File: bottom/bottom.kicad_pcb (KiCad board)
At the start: 2 copper layers, 27.5 x 37.7 mm, 5 parts, among them P1 HLW4R-2C7LF, P2 CONN_5

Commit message: Change SDA and SCL lines.
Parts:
- P1: value HLW4R-2C7LF -> CONN_4
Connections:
- P1 pad 2: /SCL -> /SDA
- P1 pad 3: /SDA -> /SCL
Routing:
- net /SDA: track 9.94 -> 13.5 mm
- net /SCL: track 13.0 -> 11.4 mm
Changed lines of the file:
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@@
     (thickness 1.6)
     (drawings 33)
-    (tracks 10)
+    (tracks 12)
     (zones 0)
     (modules 5)
@@
   )
   (setup
-    (last_trace_width 0.4064)
+    (last_trace_width 0.2032)
     (user_trace_width 0.4064)
     (trace_clearance 0.2032)
@@
       (effects (font (size 0.75 0.75) (thickness 0.15)))
     )
-    (fp_text value HLW4R-2C7LF (at 4.160001 -4.25 180) (layer F.SilkS)
+    (fp_text value CONN_4 (at 4.160001 -4.25 180) (layer F.SilkS)
       (effects (font (size 0.75 0.75) (thickness 0.15)))
     )
@@
       (net 1 /VCC))
     (pad 3 thru_hole circle (at -0.5 -5.25 270) (size 1.3 1.3) (drill 0.7) (layers *.Cu *.Mask)
+      (net 3 /SCL))
+    (pad 2 thru_hole circle (at 0.5 -3.25 270) (size 1.3 1.3) (drill 0.7) (layers *.Cu *.Mask)
       (net 2 /SDA))
-    (pad 2 thru_hole circle (at 0.5 -3.25 270) (size 1.3 1.3) (drill 0.7) (layers *.Cu *.Mask)
-      (net 3 /SCL))
     (pad 1 thru_hole circle (at 1.5 -5.25 270) (size 1.3 1.3) (drill 0.7) (layers *.Cu *.Mask)
       (net 4 /GND))
@@
   (segment (start 211.1 137.639999) (end 212.339999 136.4) (width 0.762) (layer F.Cu) (net 1))
   (segment (start 212.339999 136.4) (end 222.6 136.4) (width 0.762) (layer F.Cu) (net 1))
-  (segment (start 222.1484 139.7) (end 222.6 139.7) (width 0.2032) (layer F.Cu) (net 2))
-  (segment (start 213.1 138.639999) (end 221.088399 138.639999) (width 0.2032) (layer F.Cu) (net 2))
-  (segment (start 221.088399 138.639999) (end 222.1484 139.7) (width 0.2032) (layer F.Cu) (net 2))
-  (segment (start 222.2448 143.2) (end 222.6 143.2) (width 0.2032) (layer F.Cu) (net 3))
-  (segment (start 211.1 139.639999) (end 218.684799 139.639999) (width 0.2032) (layer F.Cu) (net 3))
-  (segment (start 218.684799 139.639999) (end 222.2448 143.2) (width 0.2032) (layer F.Cu) (net 3))
+  (segment (start 211.1 139.226893) (end 211.1 139.639999) (width 0.2032) (layer F.Cu) (net 2))
+  (segment (start 212.785893 137.541) (end 211.1 139.226893) (width 0.2032) (layer F.Cu) (net 2))
+  (segment (start 219.9894 137.541) (end 212.785893 137.541) (width 0.2032) (layer F.Cu) (net 2))
+  (segment (start 222.1484 139.7) (end 219.9894 137.541) (width 0.2032) (layer F.Cu) (net 2))
+  (segment (start 222.6 139.7) (end 222.1484 139.7) (width 0.2032) (layer F.Cu) (net 2))
+  (segment (start 217.684799 138.639999) (end 213.1 138.639999) (width 0.2032) (layer F.Cu) (net 3))
+  (segment (start 222.6 143.2) (end 222.2448 143.2) (width 0.2032) (layer F.Cu) (net 3))
+  (segment (start 222.2448 143.2) (end 217.684799 138.639999) (width 0.2032) (layer F.Cu) (net 3))
   (segment (start 213.1 140.639999) (end 218.960001 146.5) (width 0.762) (layer F.Cu) (net 4))
   (segment (start 218.960001 146.5) (end 222.6 146.5) (width 0.762) (layer F.Cu) (net 4))

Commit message: Feature connector part names on the bottom board.
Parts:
- P1: value CONN_4 -> HLW4R-2C7LF
- P2: value CONN_5 -> BP167911-05340H0A
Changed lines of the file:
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@@
-(kicad_pcb (version 20171130) (host pcbnew "(5.0.0)")
+(kicad_pcb (version 20171130) (host pcbnew 5.1.3-ffb9f22~84~ubuntu18.04.1)
   (general
     (thickness 1.6)
@@
     (zone_45_only no)
     (trace_min 0.2032)
-    (segment_width 0.2)
-    (edge_width 0.1)
     (via_size 0.889)
     (via_drill 0.635)
@@
     (uvia_min_size 0.508)
     (uvia_min_drill 0.127)
+    (edge_width 0.1)
+    (segment_width 0.2)
     (pcb_text_width 0.3)
     (pcb_text_size 1.5 1.5)
@@
     (pad_to_mask_clearance 0)
     (aux_axis_origin 0 0)
-    (visible_elements 7FFFFFFF)
+    (visible_elements 7FFFEFFF)
     (pcbplotparams
       (layerselection 0x00030_ffffffff)
@@
     (uvia_dia 0.508)
     (uvia_drill 0.127)
+    (diff_pair_width 0.2032)
     (diff_pair_gap 0.25)
-    (diff_pair_width 0.2032)
     (add_net /GND)
     (add_net /MERGE_SENSE)
@@
       (effects (font (size 0.75 0.75) (thickness 0.15)))
     )
-    (fp_text value CONN_4 (at 4.160001 -4.25 180) (layer F.SilkS)
+    (fp_text value HLW4R-2C7LF (at 4.160001 -4.25 180) (layer F.SilkS)
       (effects (font (size 0.75 0.75) (thickness 0.15)))
     )
@@
       (effects (font (size 0.75 0.75) (thickness 0.15)))
     )
-    (fp_text value CONN_5 (at 0 -9.95 180) (layer F.SilkS) hide
+    (fp_text value BP167911-05340H0A (at -4.55 -1.239999 90) (layer F.SilkS)
       (effects (font (size 0.75 0.75) (thickness 0.15)))
     )

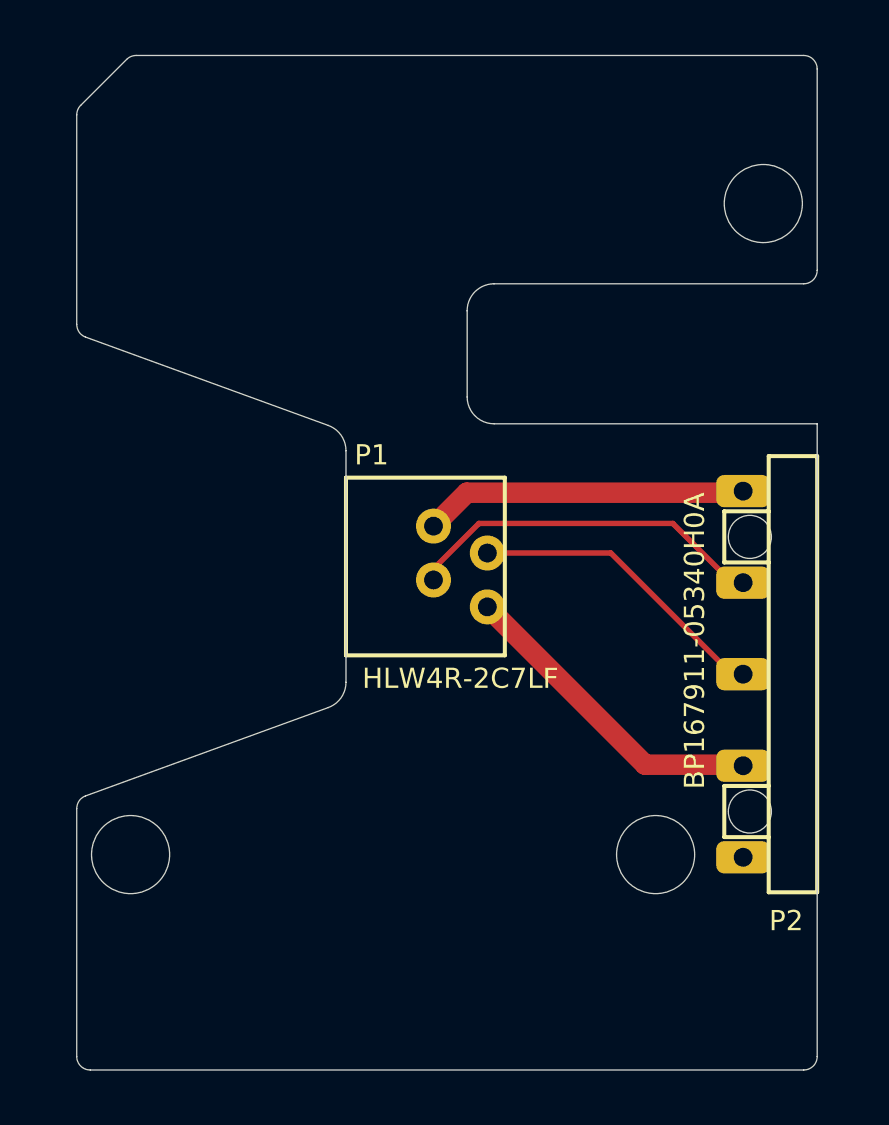
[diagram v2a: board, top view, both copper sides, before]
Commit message: Update bottom board according to new CAD files.
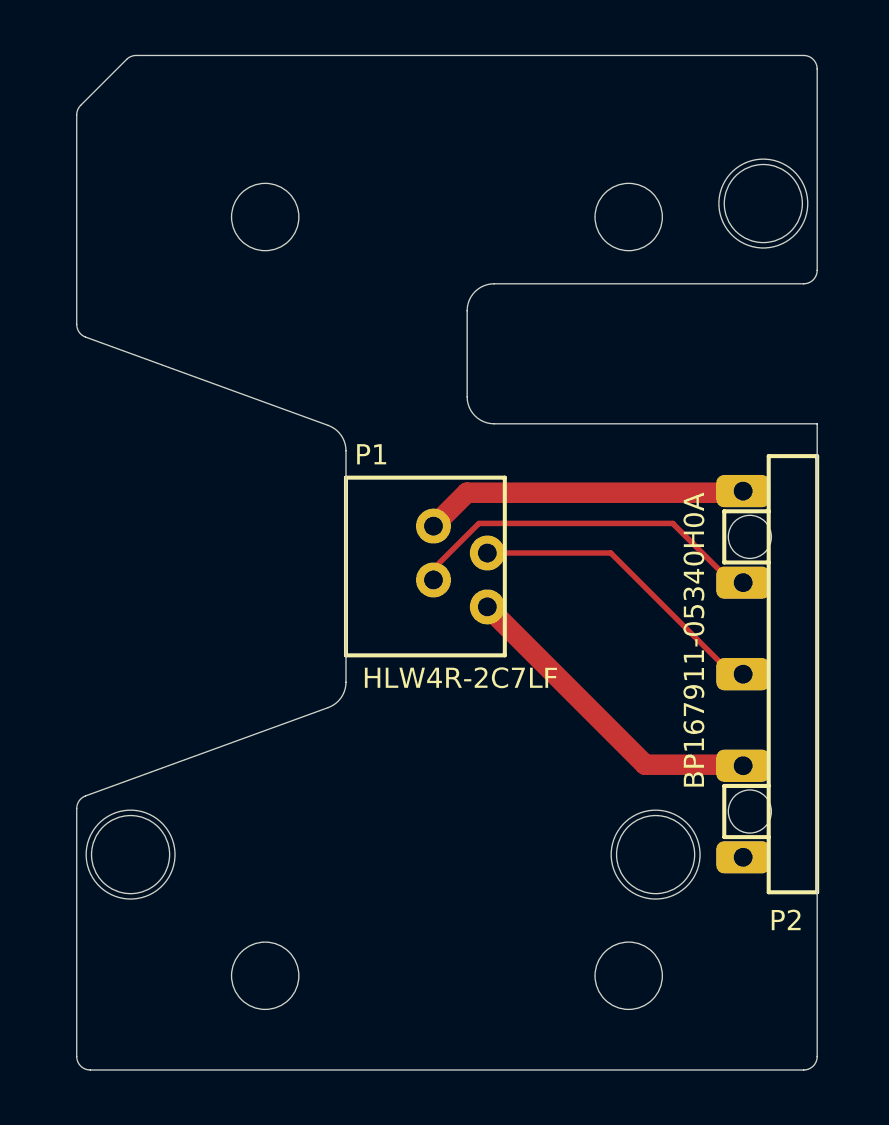
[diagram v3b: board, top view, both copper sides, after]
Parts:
- added ?: , UGL:hole_2.5mm, F.Cu at (218.3, 154.3)
- added ?: , UGL:hole_2.5mm, F.Cu at (204.8, 154.3)
- added ?: , UGL:hole_2.5mm, F.Cu at (204.8, 126.2)
- added ?: , UGL:hole_3.2999999999999545mm, F.Cu at (219.3, 149.8)
- added ?: , UGL:hole_3.2999999999999545mm, F.Cu at (199.8, 149.8)
- added ?: , UGL:hole_3.3000000000000114mm, F.Cu at (223.3, 125.7)
- added ?: , UGL:hole_2.5mm, F.Cu at (218.3, 126.2)
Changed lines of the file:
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@@
     (tracks 12)
     (zones 0)
-    (modules 5)
+    (modules 12)
     (nets 6)
   )
@@
     (pad_to_mask_clearance 0)
     (aux_axis_origin 0 0)
-    (visible_elements 7FFFEFFF)
+    (visible_elements 7FFFEF7F)
     (pcbplotparams
       (layerselection 0x00030_ffffffff)
@@
       (clearance 0.00001))
   )
-  (gr_arc (start 199.661852 122.662676) (end 197.85 123.268276) (angle -265.542362) (layer Eco1.User) (width 0.01))
+  (module UGL:hole_2.5mm locked (layer F.Cu)
+    (at 204.85 154.339996)
+    (attr virtual)
+    (fp_text reference "" (at 0 0) (layer F.SilkS)
+      (effects (font (size 1.27 1.27) (thickness 0.15)))
+    )
+    (fp_text value "" (at 0 0) (layer F.SilkS)
+      (effects (font (size 1.27 1.27) (thickness 0.15)))
+    )
+    (pad "" np_thru_hole circle (at 0 0) (size 2.5 2.5) (drill 2.5) (layers *.Cu *.Mask F.SilkS)
+      (clearance 0.00001))
+  )
+  (module UGL:hole_2.5mm locked (layer F.Cu)
+    (at 204.85 126.160004)
+    (attr virtual)
+    (fp_text reference "" (at 0 0) (layer F.SilkS)
+      (effects (font (size 1.27 1.27) (thickness 0.15)))
+    )
+    (fp_text value "" (at 0 0) (layer F.SilkS)
+      (effects (font (size 1.27 1.27) (thickness 0.15)))
+    )
+    (pad "" np_thru_hole circle (at 0 0) (size 2.5 2.5) (drill 2.5) (layers *.Cu *.Mask F.SilkS)
+      (clearance 0.00001))
+  )
+  (module UGL:hole_3.2999999999999545mm locked (layer F.Cu)
+    (at 219.35 149.839996)
+    (attr virtual)
+    (fp_text reference "" (at 0 0) (layer F.SilkS)
+      (effects (font (size 1.27 1.27) (thickness 0.15)))
+    )
+    (fp_text value "" (at 0 0) (layer F.SilkS)
+      (effects (font (size 1.27 1.27) (thickness 0.15)))
+    )
+    (pad "" np_thru_hole circle (at 0 0) (size 3.3 3.3) (drill 3.3) (layers *.Cu *.Mask F.SilkS)
+      (clearance 0.00001))
+  )
+  (module UGL:hole_3.2999999999999545mm locked (layer F.Cu)
+    (at 199.85 149.839996)
+    (attr virtual)
+    (fp_text reference "" (at 0 0) (layer F.SilkS)
+      (effects (font (size 1.27 1.27) (thickness 0.15)))
+    )
+    (fp_text value "" (at 0 0) (layer F.SilkS)
+      (effects (font (size 1.27 1.27) (thickness 0.15)))
+    )
+    (pad "" np_thru_hole circle (at 0 0) (size 3.3 3.3) (drill 3.3) (layers *.Cu *.Mask F.SilkS)
+      (clearance 0.00001))
+  )
+  (module UGL:hole_3.3000000000000114mm locked (layer F.Cu)
+    (at 223.35 125.660004)
+    (attr virtual)
+    (fp_text reference "" (at 0 0) (layer F.SilkS)
+      (effects (font (size 1.27 1.27) (thickness 0.15)))
+    )
+    (fp_text value "" (at 0 0) (layer F.SilkS)
+      (effects (font (size 1.27 1.27) (thickness 0.15)))
+    )
+    (pad "" np_thru_hole circle (at 0 0) (size 3.3 3.3) (drill 3.3) (layers *.Cu *.Mask F.SilkS)
+      (clearance 0.00001))
+  )
+  (module UGL:hole_2.5mm locked (layer F.Cu)
+    (at 218.35 126.160004)
+    (attr virtual)
+    (fp_text reference "" (at 0 0) (layer F.SilkS)
+      (effects (font (size 1.27 1.27) (thickness 0.15)))
+    )
+    (fp_text value "" (at 0 0) (layer F.SilkS)
+      (effects (font (size 1.27 1.27) (thickness 0.15)))
+    )
+    (pad "" np_thru_hole circle (at 0 0) (size 2.5 2.5) (drill 2.5) (layers *.Cu *.Mask F.SilkS)
+      (clearance 0.00001))
+  )
+  (module UGL:hole_2.5mm locked (layer F.Cu)
+    (at 218.35 154.339996)
+    (attr virtual)
+    (fp_text reference "" (at 0 0) (layer F.SilkS)
+      (effects (font (size 1.27 1.27) (thickness 0.15)))
+    )
+    (fp_text value "" (at 0 0) (layer F.SilkS)
+      (effects (font (size 1.27 1.27) (thickness 0.15)))
+    )
+    (pad "" np_thru_hole circle (at 0 0) (size 2.5 2.5) (drill 2.5) (layers *.Cu *.Mask F.SilkS)
+      (clearance 0.00001))
+  )
   (gr_circle (center 223.35 125.660004) (end 223.35 127.310004) (layer Eco1.User) (width 0.01))
   (gr_text "PCB ID: touchpad_bottom_1.0.0" (at 212 156.8) (layer B.SilkS)
@@
   (gr_circle (center 219.35 149.839996) (end 219.35 151.489996) (layer Eco1.User) (width 0.01))
   (gr_circle (center 199.85 149.839996) (end 199.85 151.489996) (layer Eco1.User) (width 0.01))
-  (gr_circle (center 223.35 122.059998) (end 223.35 123.959998) (layer Eco1.User) (width 0.01))
-  (gr_circle (center 223.35 155.339996) (end 223.35 157.239996) (layer Eco1.User) (width 0.01))
-  (gr_arc (start 199.666942 155.331772) (end 197.85 155.948276) (angle -322.8371138) (layer Eco1.User) (width 0.01))
+  (gr_circle (center 204.85 154.339996) (end 206.75 154.339996) (layer Eco1.User) (width 0.01))
+  (gr_circle (center 204.85 126.160004) (end 206.75 126.160004) (layer Eco1.User) (width 0.01))
+  (gr_circle (center 218.35 126.160004) (end 220.25 126.160004) (layer Eco1.User) (width 0.01))
+  (gr_circle (center 218.35 154.339996) (end 220.25 154.339996) (layer Eco1.User) (width 0.01))
   (segment (start 211.1 137.639999) (end 212.339999 136.4) (width 0.762) (layer F.Cu) (net 1))
   (segment (start 212.339999 136.4) (end 222.6 136.4) (width 0.762) (layer F.Cu) (net 1))

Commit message: Add UHK logos.
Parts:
- added G***: LOGO, ugl:UHK_Logo_12x3.4_mm, B.Cu at (209.8, 149.8)
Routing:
- added copper zone on B.Cu, net (none)
